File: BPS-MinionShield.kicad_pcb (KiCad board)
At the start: 2 copper layers, 85 x 66 mm, 44 parts, among them J1 TempConn2, J10 TempConn9, J11 TempConn10, J12 TempConn11, J13 TempConn12, J14 TempConn2, J15 TempConn13, J16 TempConn14, J17 TempConn15, J18 TempConn16, J2 TempConn3, J3 TempConn4, J4 TempConn5, J5 TempConn6, J6 TempConn7, J7 TempConn1, J8 TempConn8, J9 TempConn2

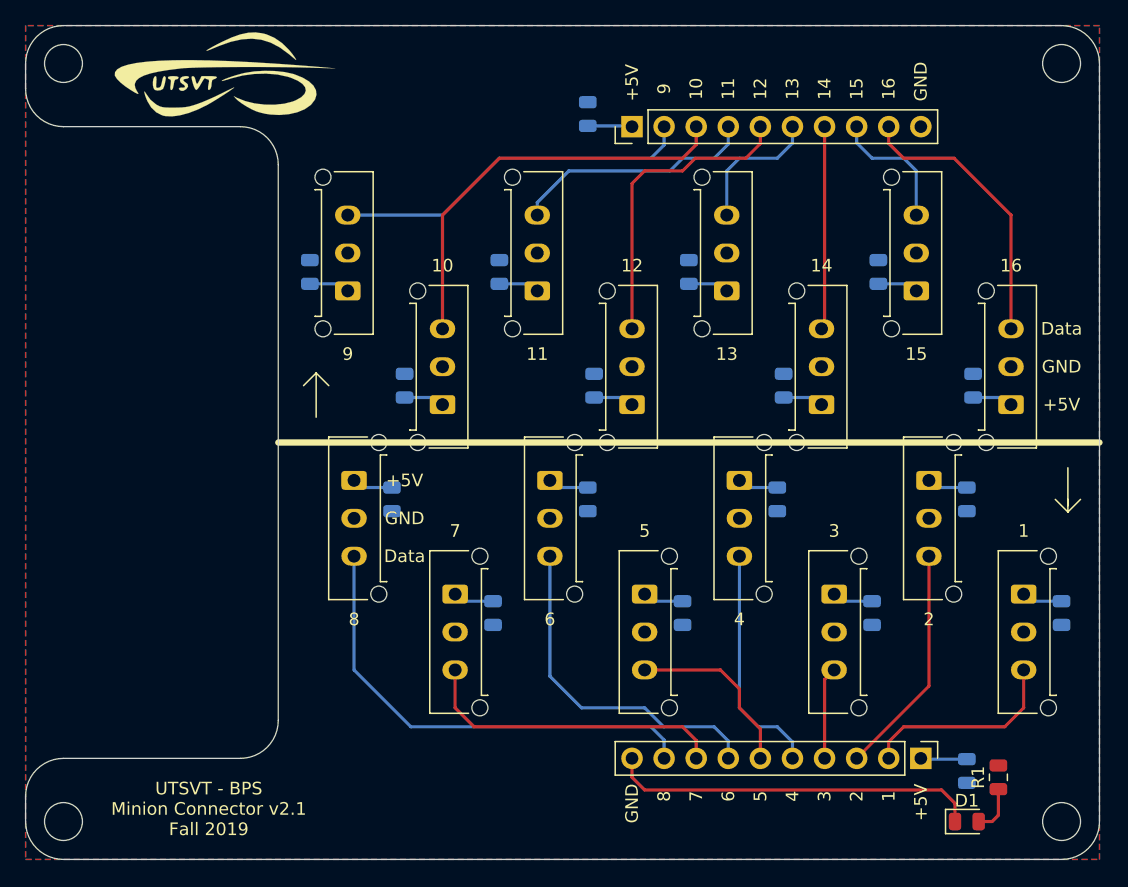
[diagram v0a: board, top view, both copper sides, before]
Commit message: finished PCB layout with a displayport connector for thermistors
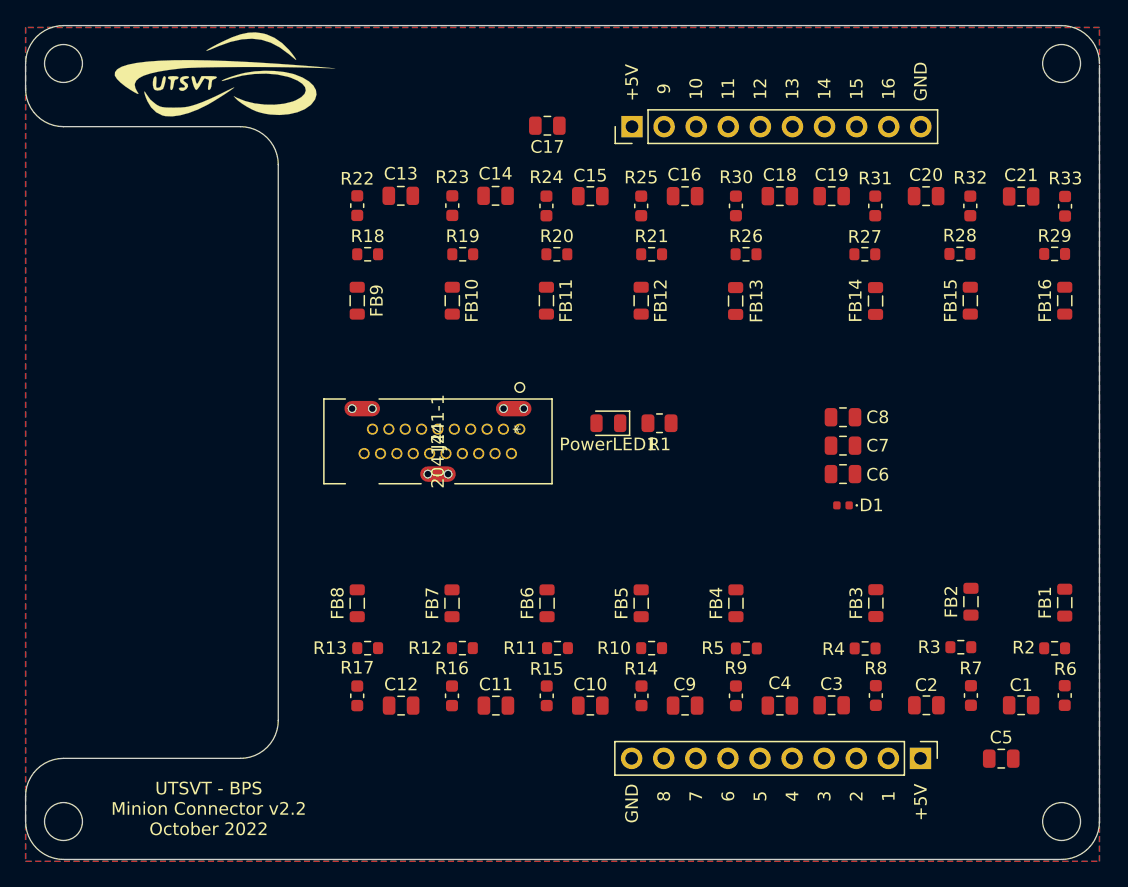
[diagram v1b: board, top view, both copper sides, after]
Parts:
- removed the J1 at (171.5, 106.0)
- removed J10: TempConn9, Connector_Molex:Molex_Micro-Fit_3.0_43650-0315_1x03_P3.00mm_Vertical
- removed J11: TempConn10, Connector_Molex:Molex_Micro-Fit_3.0_43650-0315_1x03_P3.00mm_Vertical
- removed J12: TempConn11, Connector_Molex:Molex_Micro-Fit_3.0_43650-0315_1x03_P3.00mm_Vertical
- removed J13: TempConn12, Connector_Molex:Molex_Micro-Fit_3.0_43650-0315_1x03_P3.00mm_Vertical
- removed J15: TempConn13, Connector_Molex:Molex_Micro-Fit_3.0_43650-0315_1x03_P3.00mm_Vertical
- removed J16: TempConn14, Connector_Molex:Molex_Micro-Fit_3.0_43650-0315_1x03_P3.00mm_Vertical
- removed J17: TempConn15, Connector_Molex:Molex_Micro-Fit_3.0_43650-0315_1x03_P3.00mm_Vertical
- removed J18: TempConn16, Connector_Molex:Molex_Micro-Fit_3.0_43650-0315_1x03_P3.00mm_Vertical
- removed the J3 at (156.5, 106.0)
- removed J4: TempConn5, Connector_Molex:Molex_Micro-Fit_3.0_43650-0315_1x03_P3.00mm_Vertical
- removed J5: TempConn6, Connector_Molex:Molex_Micro-Fit_3.0_43650-0315_1x03_P3.00mm_Vertical
- removed J6: TempConn7, Connector_Molex:Molex_Micro-Fit_3.0_43650-0315_1x03_P3.00mm_Vertical
- removed J7: TempConn1, Connector_Molex:Molex_Micro-Fit_3.0_43650-0315_1x03_P3.00mm_Vertical
- removed J8: TempConn8, Connector_Molex:Molex_Micro-Fit_3.0_43650-0315_1x03_P3.00mm_Vertical
- added C19: 1u, Capacitor_SMD:C_0805_2012Metric, F.Cu at (163.8, 83.5)
- added C20: 1u, Capacitor_SMD:C_0805_2012Metric, F.Cu at (171.3, 83.5)
- added C21: 1u, Capacitor_SMD:C_0805_2012Metric, F.Cu at (178.8, 83.5)
- added FB1: 2.2k, Inductor_SMD:L_0805_2012Metric, F.Cu at (182.2, 115.7)
- added FB10: 2.2k, Inductor_SMD:L_0805_2012Metric, F.Cu at (133.8, 91.8)
- added FB11: 2.2k, Inductor_SMD:L_0805_2012Metric, F.Cu at (141.2, 91.8)
- added FB12: 2.2k, Inductor_SMD:L_0805_2012Metric, F.Cu at (148.7, 91.8)
- added FB13: 2.2k, Inductor_SMD:L_0805_2012Metric, F.Cu at (156.2, 91.8)
- added FB14: 2.2k, Inductor_SMD:L_0805_2012Metric, F.Cu at (167.3, 91.8)
- added FB15: 2.2k, Inductor_SMD:L_0805_2012Metric, F.Cu at (174.8, 91.8)
- added FB16: 2.2k, Inductor_SMD:L_0805_2012Metric, F.Cu at (182.2, 91.8)
- added FB2: 2.2k, Inductor_SMD:L_0805_2012Metric, F.Cu at (174.8, 115.6)
- added FB3: 2.2k, Inductor_SMD:L_0805_2012Metric, F.Cu at (167.3, 115.7)
- added FB4: 2.2k, Inductor_SMD:L_0805_2012Metric, F.Cu at (156.2, 115.7)
- added FB5: 2.2k, Inductor_SMD:L_0805_2012Metric, F.Cu at (148.7, 115.7)
- added FB6: 2.2k, Inductor_SMD:L_0805_2012Metric, F.Cu at (141.3, 115.7)
- added FB7: 2.2k, Inductor_SMD:L_0805_2012Metric, F.Cu at (133.8, 115.7)
- added FB8: 2.2k, Inductor_SMD:L_0805_2012Metric, F.Cu at (126.2, 115.7)
- added FB9: 2.2k, Inductor_SMD:L_0805_2012Metric, F.Cu at (126.2, 91.8)
- added PowerLED1: Green, LED_SMD:LED_0805_2012Metric, F.Cu at (146.1, 101.5)
- added R10: 10k, Resistor_SMD:R_0603_1608Metric, F.Cu at (149.6, 119.3)
- added R11: 10k, Resistor_SMD:R_0603_1608Metric, F.Cu at (142.1, 119.3)
- added R12: 10k, Resistor_SMD:R_0603_1608Metric, F.Cu at (134.6, 119.3)
- added R13: 10k, Resistor_SMD:R_0603_1608Metric, F.Cu at (127.1, 119.3)
- added R14: 4.7k, Capacitor_SMD:C_0603_1608Metric, F.Cu at (148.8, 123.0)
- added R15: 4.7k, Capacitor_SMD:C_0603_1608Metric, F.Cu at (141.2, 123.0)
- added R16: 4.7k, Capacitor_SMD:C_0603_1608Metric, F.Cu at (133.8, 123.0)
- added R17: 4.7k, Capacitor_SMD:C_0603_1608Metric, F.Cu at (126.2, 123.0)
- added R18: 10k, Resistor_SMD:R_0603_1608Metric, F.Cu at (127.1, 88.1)
- added R19: 10k, Resistor_SMD:R_0603_1608Metric, F.Cu at (134.6, 88.1)
- added R2: 10k, Resistor_SMD:R_0603_1608Metric, F.Cu at (181.4, 119.3)
- added R20: 10k, Resistor_SMD:R_0603_1608Metric, F.Cu at (142.1, 88.1)
- added R21: 10k, Resistor_SMD:R_0603_1608Metric, F.Cu at (149.6, 88.1)
- added R22: 4.7k, Capacitor_SMD:C_0603_1608Metric, F.Cu at (126.2, 84.2)
- added R23: 4.7k, Capacitor_SMD:C_0603_1608Metric, F.Cu at (133.8, 84.2)
- added R24: 4.7k, Capacitor_SMD:C_0603_1608Metric, F.Cu at (141.2, 84.3)
- added R25: 4.7k, Capacitor_SMD:C_0603_1608Metric, F.Cu at (148.7, 84.3)
- added R26: 10k, Resistor_SMD:R_0603_1608Metric, F.Cu at (157.0, 88.1)
- added R27: 10k, Resistor_SMD:R_0603_1608Metric, F.Cu at (166.4, 88.1)
- added R28: 10k, Resistor_SMD:R_0603_1608Metric, F.Cu at (173.9, 88.1)
- added R29: 10k, Resistor_SMD:R_0603_1608Metric, F.Cu at (181.4, 88.1)
- added R3: 10k, Resistor_SMD:R_0603_1608Metric, F.Cu at (174.0, 119.2)
- added R30: 4.7k, Capacitor_SMD:C_0603_1608Metric, F.Cu at (156.2, 84.3)
- added R31: 4.7k, Capacitor_SMD:C_0603_1608Metric, F.Cu at (167.2, 84.3)
- added R32: 4.7k, Capacitor_SMD:C_0603_1608Metric, F.Cu at (174.8, 84.3)
- added R33: 4.7k, Capacitor_SMD:C_0603_1608Metric, F.Cu at (182.3, 84.3)
- added R4: 10k, Resistor_SMD:R_0603_1608Metric, F.Cu at (166.4, 119.3)
- added R5: 10k, Resistor_SMD:R_0603_1608Metric, F.Cu at (157.1, 119.3)
- added R6: 4.7k, Capacitor_SMD:C_0603_1608Metric, F.Cu at (182.2, 123.0)
- added R7: 4.7k, Capacitor_SMD:C_0603_1608Metric, F.Cu at (174.8, 123.0)
- added R8: 4.7k, Capacitor_SMD:C_0603_1608Metric, F.Cu at (167.3, 123.0)
- added R9: 4.7k, Capacitor_SMD:C_0603_1608Metric, F.Cu at (156.2, 123.0)
- C1, C10, C11, C12, C13, C14, C15, C16, C18, C2, C3, C4, C7, C9: value 100n -> 1u; moved to F.Cu
- C17, C5, C6: moved to F.Cu
- C8: value 100n -> 10u; moved to F.Cu
- D1: value Green -> D_TVS; footprint LED_SMD:LED_0805_2012Metric -> Diode_SMD:D_0402_1005Metric
- J1: renamed from J9; value TempConn2 -> TempConn1
- J2: value TempConn3 -> 2041441-1; footprint Connector_Molex:Molex_Micro-Fit_3.0_43650-0315_1x03_P3.00mm_Vertical -> UTSVT_Connectors:2041441-1
- moved C17 60.9 mm to (141.3, 77.9), turned to 180 degrees
- moved R1 38.8 mm to (150.2, 101.5), turned to 180 degrees
- moved C3 34.5 mm to (163.8, 123.8), turned to 0 degrees
- moved C11 34.3 mm to (137.2, 123.8), turned to 180 degrees
- moved C5 34.2 mm to (177.2, 128.0), turned to 0 degrees
- moved C14 33.0 mm to (137.2, 83.5), turned to 180 degrees
- moved C16 30.3 mm to (152.2, 83.5), turned to 180 degrees
- moved C15 28.7 mm to (144.7, 83.5), turned to 180 degrees
- moved J2 28.1 mm to (139.1, 101.9), turned to 90 degrees
- moved D1 26.9 mm to (164.7, 108.0), turned to 180 degrees
- moved C9 26.3 mm to (152.2, 123.8), turned to 180 degrees
- moved C1 25.6 mm to (178.8, 123.8), turned to 0 degrees
- moved C4 22.0 mm to (159.7, 123.8), turned to 180 degrees
- moved C12 22.0 mm to (129.7, 123.8), turned to 180 degrees
- moved C7 18.4 mm to (164.7, 103.2), turned to 0 degrees
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- renumbered J14 to J3
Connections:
- C1 pad 2: +5V -> /TempSens1
- C10 pad 1: +5V -> GND
- C10 pad 2: GND -> /TempSens6
- C11 pad 2: +5V -> /TempSens7
- C12 pad 2: +5V -> /TempSens8
- C13 pad 2: +5V -> /TempSens9
- C14 pad 2: +5V -> /TempSens10
- C15 pad 2: +5V -> /TempSens11
- C16 pad 2: +5V -> /TempSens12
- C17 pad 1: GND -> +5V
- C17 pad 2: +5V -> GND
- C18 pad 2: +5V -> /TempSens13
- C2 pad 2: +5V -> /TempSens2
- C3 pad 2: +5V -> /TempSens3
- C4 pad 2: +5V -> /TempSens4
- C9 pad 2: +5V -> /TempSens5
- D1 pad 1: GND -> +5V
- D1 pad 2: Net-(D1-Pad2) -> GND
- J2 pad 1: +5V -> /temp1
- J2 pad 2: GND -> /temp2
- J2 pad 3: /TempSens3 -> /temp3
- R1 pad 2: Net-(D1-Pad2) -> Net-(PowerLED1-Pad2)
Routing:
- net +5V: track 60.4 -> 0.18 mm
- net /TempSens8: track 37.3 -> 0.00 mm
- net /TempSens10: track 32.8 -> 0.00 mm
- net GND: track 29.4 -> 0.00 mm
- net /TempSens9: track 28.8 -> 0.00 mm
- net /TempSens6: track 27.1 -> 0.00 mm
- net /TempSens7: track 24.6 -> 0.00 mm
- net /TempSens12: track 24.3 -> 0.00 mm
- net /TempSens16: track 22.4 -> 0.00 mm
- net /TempSens11: track 19.4 -> 0.00 mm
- net /TempSens4: track 18.6 -> 0.00 mm
- net /TempSens2: track 18.4 -> 0.00 mm
- net /TempSens1: track 16.1 -> 0.00 mm
- net /TempSens14: track 16.4 -> 0.34 mm
- net /TempSens5: track 14.3 -> 0.00 mm
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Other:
- outline, holes or cut-outs redrawn
- net class Default removed
- board text added: "UTSVT - BPS Minion Connector v2.2 October 2022"
- board text removed: "Data"
- board text removed: "UTSVT - BPS Minion Connector v2.1 Fall 2019"

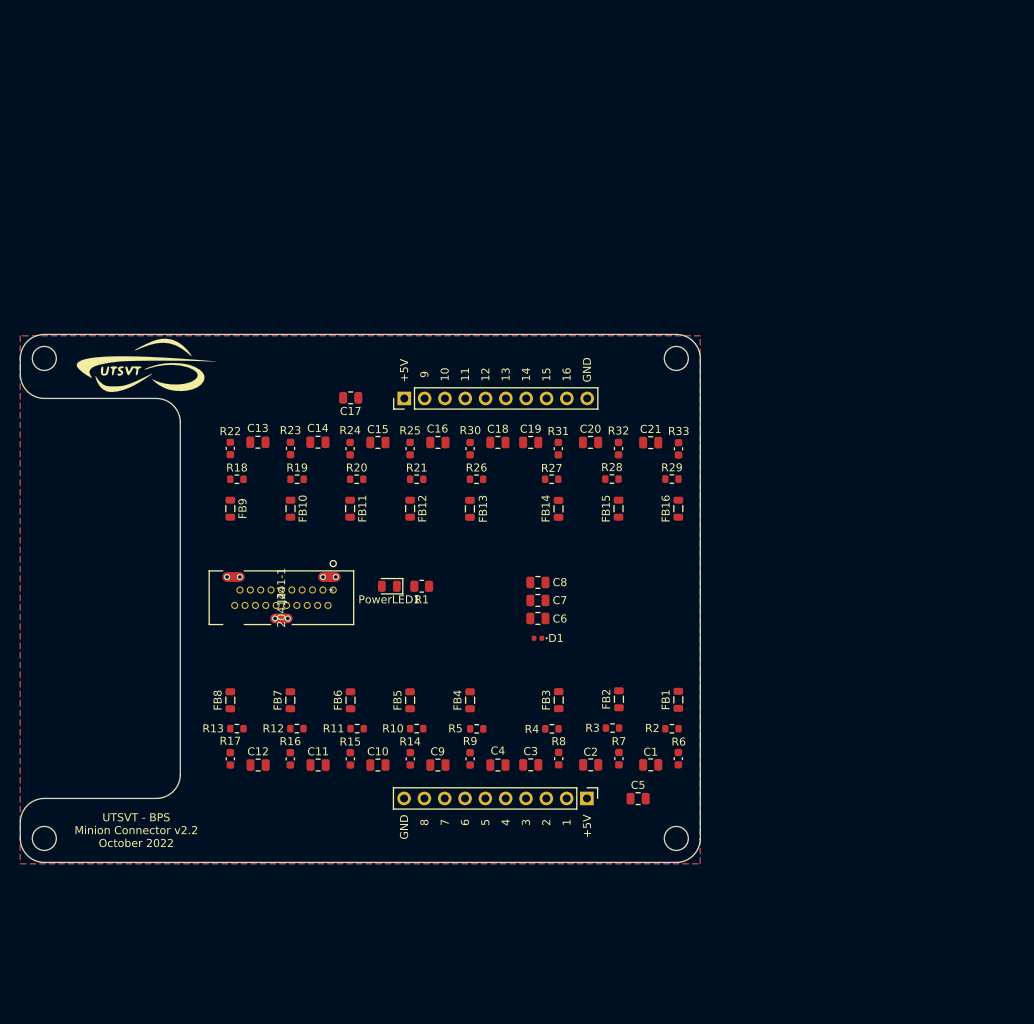
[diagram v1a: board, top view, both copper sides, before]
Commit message: added orion connector footprint
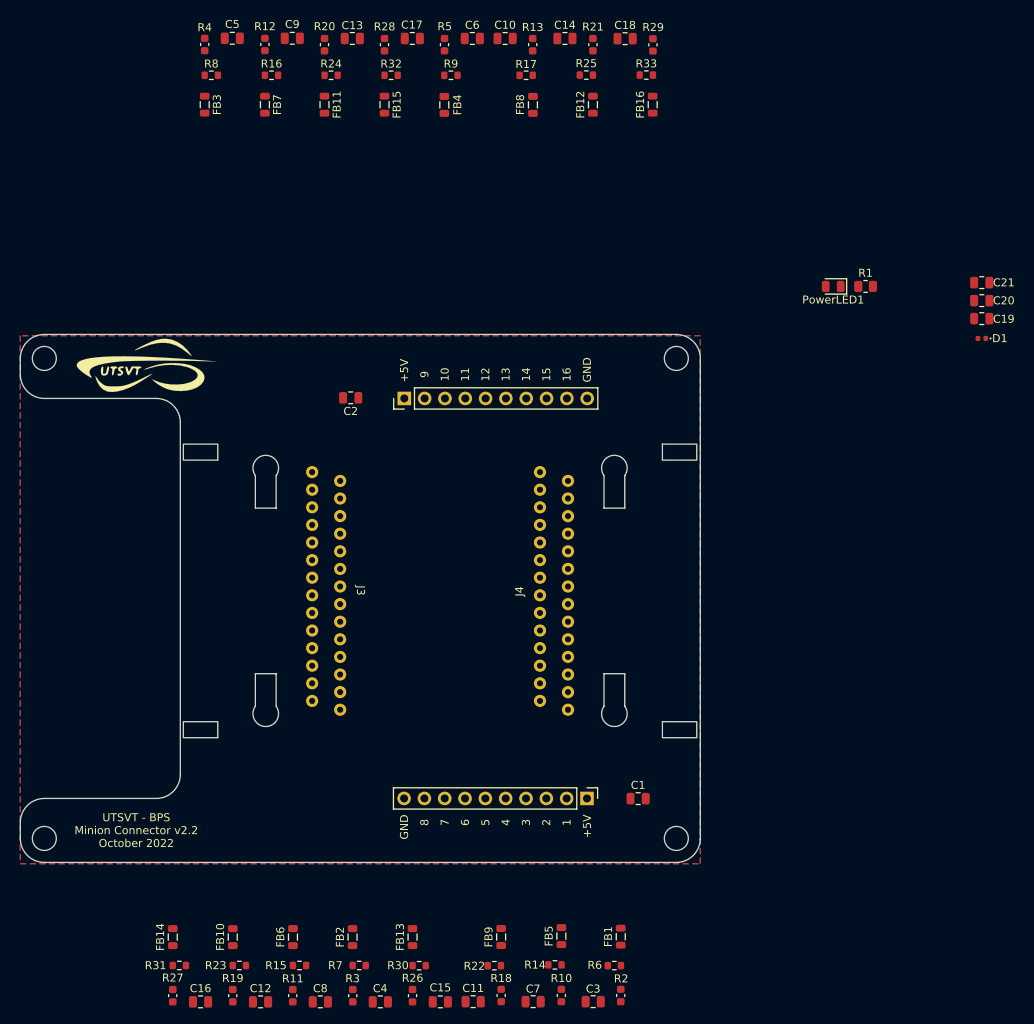
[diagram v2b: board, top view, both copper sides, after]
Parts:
- removed the J2 at (139.1, 101.9)
- added J3: Conn_01x28_Female, UTSVT_Connectors:MX34028SF1, F.Cu at (140.0, 116.9)
- added J4: Conn_01x28_Female, UTSVT_Connectors:MX34028SF1, F.Cu at (165.0, 87.2)
- moved C21 67.0 mm to (220.2, 63.5)
- moved C19 67.0 mm to (220.2, 68.0)
- moved C20 67.0 mm to (220.2, 65.8)
- moved D1 67.0 mm to (220.2, 70.5)
- moved PowerLED1 67.0 mm to (201.6, 64.0)
- moved R1 67.0 mm to (205.7, 64.0)
- moved C18 50.6 mm to (175.6, 33.0)
- moved FB11 50.6 mm to (138.0, 41.3)
- moved FB12 50.6 mm to (171.6, 41.3)
- moved FB15 50.6 mm to (145.5, 41.3)
- moved FB16 50.6 mm to (179.1, 41.3)
- moved FB3 50.6 mm to (123.0, 41.3)
- moved FB7 50.6 mm to (130.6, 41.3)
- moved R13 50.6 mm to (164.1, 33.8)
- moved R20 50.6 mm to (138.0, 33.8)
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- renumbered C5 to C1, C19 to C10, C3 to C11, C11 to C12, C15 to C13, C20 to C14, C4 to C15, C12 to C16, C16 to C17, C21 to C18, C6 to C19, C17 to C2, C7 to C20, C8 to C21, C1 to C3, C9 to C4, C13 to C5, C18 to C6, C2 to C7, C10 to C8, C14 to C9, FB7 to FB10, FB15 to FB12, FB4 to FB13, FB8 to FB14, FB12 to FB15, FB5 to FB2, FB9 to FB3, FB13 to FB4, FB2 to FB5, FB10 to FB7, FB14 to FB8, FB3 to FB9, H3 to H2, H2 to H3, J3 to J2, R7 to R10, R15 to R11, R23 to R12, R31 to R13, R3 to R14, R11 to R15, R19 to R16, R27 to R17, R8 to R18, R16 to R19, R6 to R2, R24 to R20, R32 to R21, R4 to R22, R12 to R23, R20 to R24, R28 to R25, R9 to R26, R17 to R27, R25 to R28, R33 to R29, R14 to R3, R5 to R30, R13 to R31, R21 to R32, R29 to R33, R22 to R4, R30 to R5, R2 to R6, R10 to R7, R18 to R8, R26 to R9

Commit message: new footprint from temp expansion module
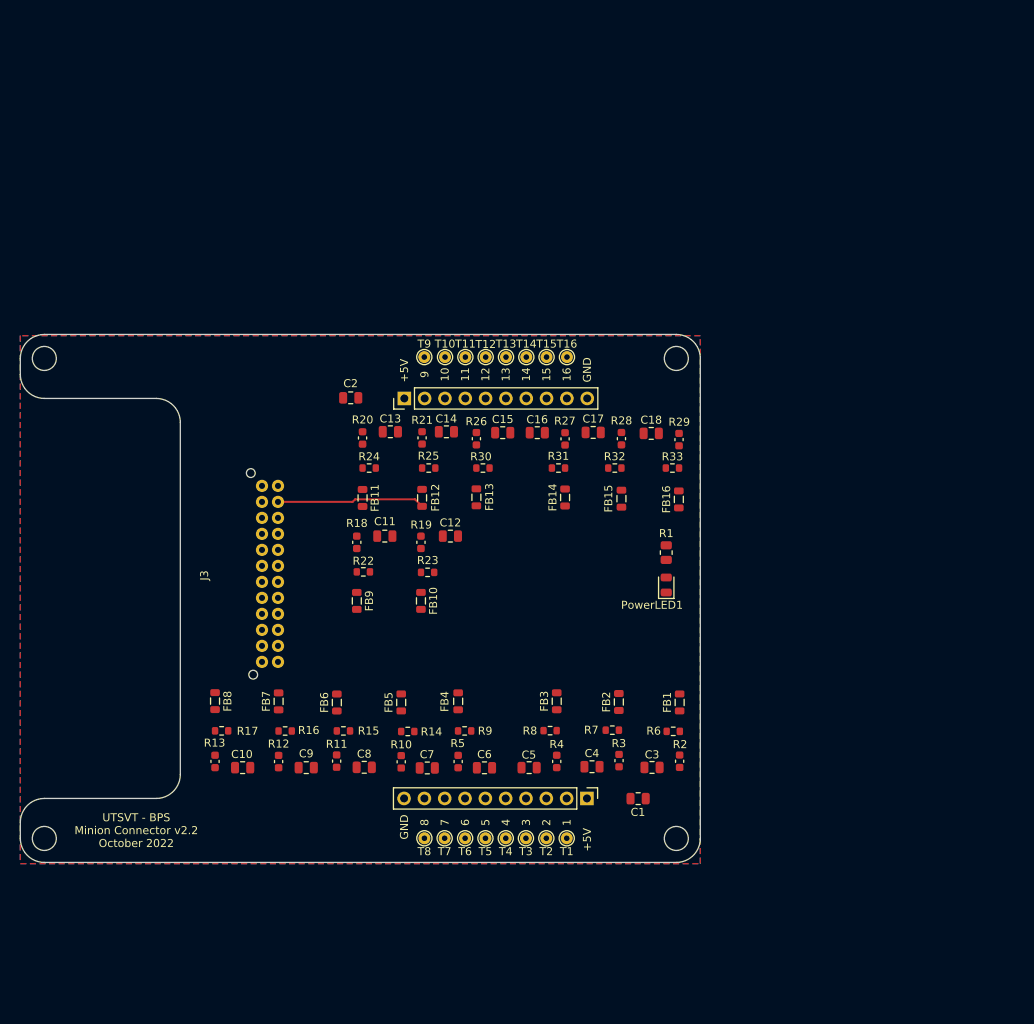
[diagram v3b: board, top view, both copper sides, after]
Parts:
- removed C19: 100n, Capacitor_SMD:C_0805_2012Metric
- removed C20: 1u, Capacitor_SMD:C_0805_2012Metric
- removed C21: 10u, Capacitor_SMD:C_0805_2012Metric
- removed D1: D_TVS, Diode_SMD:D_0402_1005Metric
- removed G***: LOGO, UTSVT_Special:UTSVT_Logo_Symbol
- removed G***: LOGO, UTSVT_Special:Hallock_Image_Tiny
- removed J4: Conn_01x28_Female, UTSVT_Connectors:MX34028SF1
- added T1: TestPoint, TestPoint:TestPoint_THTPad_D1.5mm_Drill0.7mm, F.Cu at (168.3, 133.0)
- added T10: TestPoint, TestPoint:TestPoint_THTPad_D1.5mm_Drill0.7mm, F.Cu at (153.1, 72.8)
- added T11: TestPoint, TestPoint:TestPoint_THTPad_D1.5mm_Drill0.7mm, F.Cu at (155.6, 72.8)
- added T12: TestPoint, TestPoint:TestPoint_THTPad_D1.5mm_Drill0.7mm, F.Cu at (158.2, 72.8)
- added T13: TestPoint, TestPoint:TestPoint_THTPad_D1.5mm_Drill0.7mm, F.Cu at (160.7, 72.8)
- added T14: TestPoint, TestPoint:TestPoint_THTPad_D1.5mm_Drill0.7mm, F.Cu at (163.2, 72.8)
- added T15: TestPoint, TestPoint:TestPoint_THTPad_D1.5mm_Drill0.7mm, F.Cu at (165.8, 72.8)
- added T16: TestPoint, TestPoint:TestPoint_THTPad_D1.5mm_Drill0.7mm, F.Cu at (168.3, 72.8)
- added T2: TestPoint, TestPoint:TestPoint_THTPad_D1.5mm_Drill0.7mm, F.Cu at (165.8, 133.0)
- added T3: TestPoint, TestPoint:TestPoint_THTPad_D1.5mm_Drill0.7mm, F.Cu at (163.2, 133.0)
- added T4: TestPoint, TestPoint:TestPoint_THTPad_D1.5mm_Drill0.7mm, F.Cu at (160.7, 133.0)
- added T5: TestPoint, TestPoint:TestPoint_THTPad_D1.5mm_Drill0.7mm, F.Cu at (158.1, 133.0)
- added T6: TestPoint, TestPoint:TestPoint_THTPad_D1.5mm_Drill0.7mm, F.Cu at (155.6, 133.0)
- added T7: TestPoint, TestPoint:TestPoint_THTPad_D1.5mm_Drill0.7mm, F.Cu at (153.0, 133.0)
- added T8: TestPoint, TestPoint:TestPoint_THTPad_D1.5mm_Drill0.7mm, F.Cu at (150.5, 133.0)
- added T9: TestPoint, TestPoint:TestPoint_THTPad_D1.5mm_Drill0.7mm, F.Cu at (150.5, 72.8)
- J3: value Conn_01x28_Female -> Conn_01x24_Female; footprint UTSVT_Connectors:MX34028SF1 -> UTSVT_Connectors:PADP-24V-1-S
- moved R4 99.8 mm to (167.1, 123.4), turned to 90 degrees
- moved C5 98.4 mm to (163.6, 124.2), turned to 0 degrees
- moved R13 98.0 mm to (124.3, 123.4), turned to 90 degrees
- moved C10 96.9 mm to (127.8, 124.2), turned to 180 degrees
- moved R8 92.2 mm to (166.2, 119.5), turned to 180 degrees
- moved C9 91.2 mm to (135.7, 124.2)
- moved C6 91.2 mm to (158.0, 124.2)
- moved R17 90.4 mm to (125.2, 119.5), turned to 0 degrees
- moved R12 89.7 mm to (132.3, 123.4), turned to 90 degrees
- moved R5 89.6 mm to (154.7, 123.4), turned to 90 degrees
- moved FB3 86.6 mm to (167.1, 115.8), turned to 90 degrees
- moved R27 85.1 mm to (168.1, 83.1), turned to -90 degrees
- moved FB8 84.5 mm to (124.3, 115.8), turned to 90 degrees
- moved C16 82.7 mm to (164.6, 82.3), turned to 0 degrees
- moved R16 82.0 mm to (133.1, 119.6)
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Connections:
- C10 pad 2: /TempSens14 -> /TempSens8
- C11 pad 2: /TempSens3 -> /TempSens9
- C12 pad 2: /TempSens7 -> /TempSens10
- C14 pad 2: /TempSens15 -> /TempSens12
- C15 pad 2: /TempSens4 -> /TempSens13
- C16 pad 2: /TempSens8 -> /TempSens14
- C17 pad 2: /TempSens12 -> /TempSens15
- C4 pad 2: /TempSens5 -> /TempSens2
- C5 pad 2: /TempSens9 -> /TempSens3
- C6 pad 2: /TempSens13 -> /TempSens4
- C7 pad 2: /TempSens2 -> /TempSens5
- C9 pad 2: /TempSens10 -> /TempSens7
- J3 pad 1: unconnected-(J3-Pad1) -> GND
- J3 pad 10: /temp3 -> unconnected-(J3-Pad10)
- J3 pad 11: /temp2 -> /temp11
- J3 pad 12: /temp1 -> unconnected-(J3-Pad12)
- J3 pad 13: unconnected-(J3-Pad13) -> GND
- J3 pad 14: unconnected-(J3-Pad14) -> GND
- J3 pad 15: unconnected-(J3-Pad15) -> /temp10
- J3 pad 16: unconnected-(J3-Pad16) -> /temp1
- J3 pad 17: unconnected-(J3-Pad17) -> /temp9
- J3 pad 18: unconnected-(J3-Pad18) -> /temp2
- J3 pad 19: GND -> /temp3
- J3 pad 2: unconnected-(J3-Pad2) -> GND
- J3 pad 20: GND -> /temp8
- J3 pad 21: GND -> /temp4
- J3 pad 22: GND -> /temp7
- J3 pad 23: GND -> /temp5
- J3 pad 24: GND -> /temp6
- J3 pad 3: unconnected-(J3-Pad3) -> /temp15
- J3 pad 4: unconnected-(J3-Pad4) -> /temp16
- J3 pad 5: /temp8 -> /temp14
- J3 pad 6: /temp7 -> unconnected-(J3-Pad6)
- J3 pad 7: /temp6 -> /temp13
- J3 pad 8: /temp5 -> unconnected-(J3-Pad8)
- J3 pad 9: /temp4 -> /temp12
- R10 pad 1: /TempSens2 -> /TempSens5
- R12 pad 1: /TempSens10 -> /TempSens7
- R13 pad 1: /TempSens14 -> /TempSens8
- R18 pad 1: /TempSens3 -> /TempSens9
- R19 pad 1: /TempSens7 -> /TempSens10
- R21 pad 1: /TempSens15 -> /TempSens12
- R26 pad 1: /TempSens4 -> /TempSens13
- R27 pad 1: /TempSens8 -> /TempSens14
- R28 pad 1: /TempSens12 -> /TempSens15
- R3 pad 1: /TempSens5 -> /TempSens2
- R4 pad 1: /TempSens9 -> /TempSens3
- R5 pad 1: /TempSens13 -> /TempSens4
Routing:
- net /temp15: track 0.00 -> 18.5 mm
